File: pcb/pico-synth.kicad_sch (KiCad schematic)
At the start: 48 parts

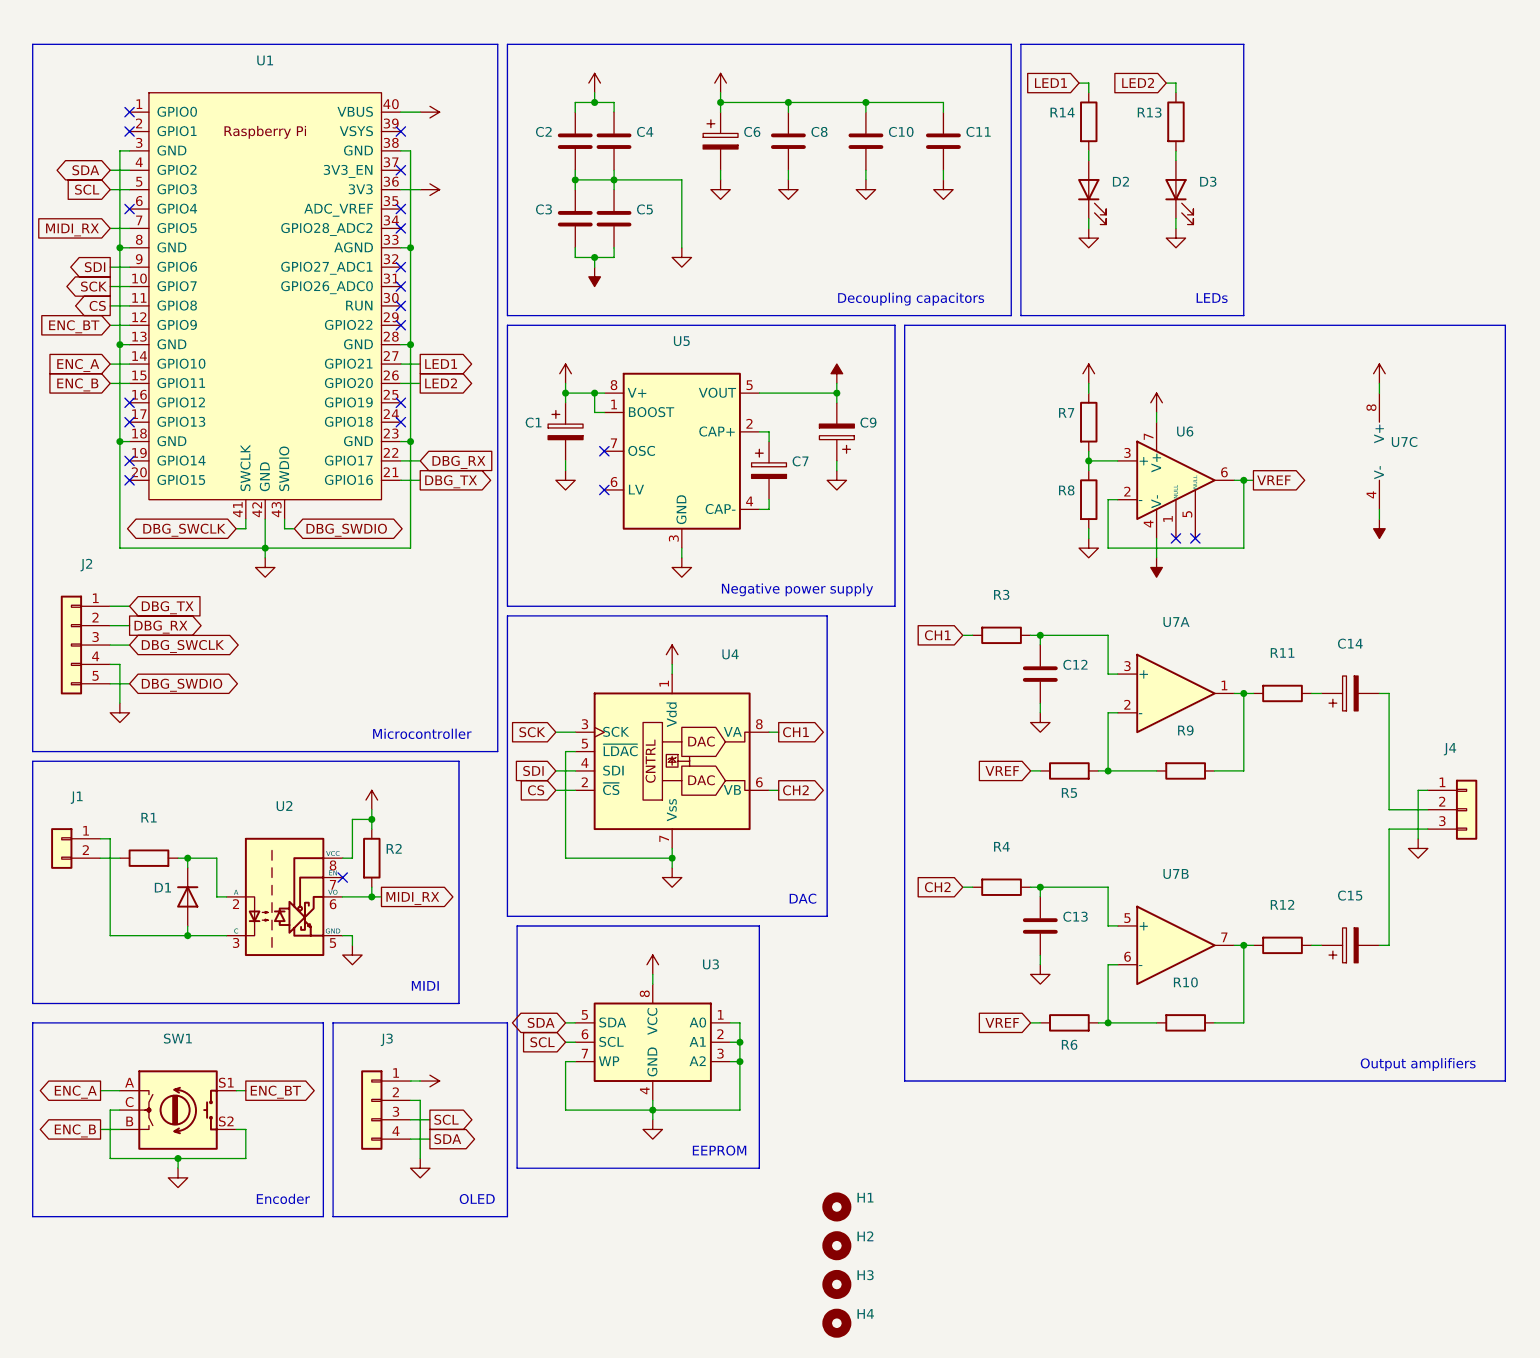
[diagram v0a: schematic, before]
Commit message: pcb: added new revision 2.2
trying to avoid using dc-dc charge pump
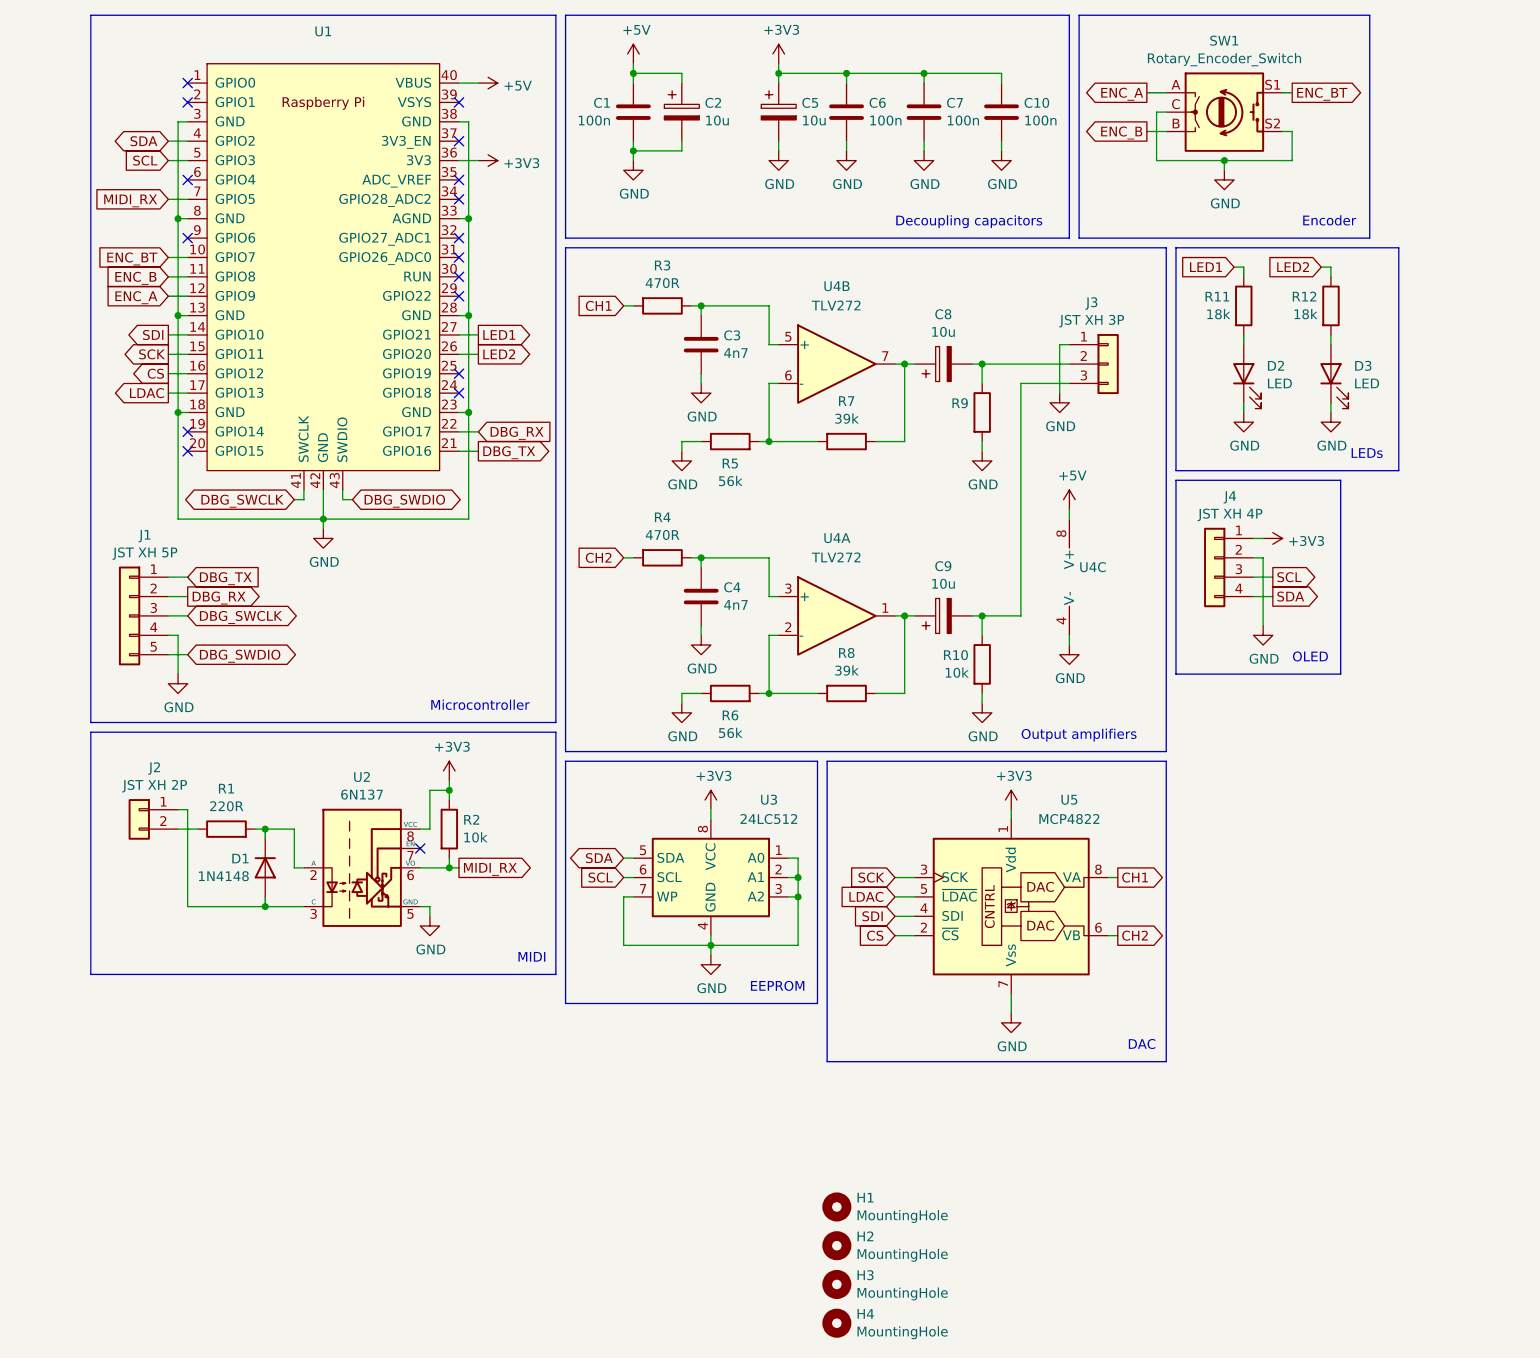
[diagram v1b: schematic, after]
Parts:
- removed C1, C14, C15, C7: (no value), symbol Device:CP
- removed C3, C4, C5: (no value), symbol Device:C
- removed R11, R12, R7, R8: (no value), symbol Device:R
- removed U5: (no value), symbol Regulator_SwitchedCapacitor:LTC1044
- removed U6: (no value), symbol Amplifier_Operational:TL071
- removed U7: (no value), symbol Amplifier_Operational:TL072
- added C2, C8: 10u, Capacitor_THT:CP_Radial_D5.0mm_P2.50mm, symbol Device:CP
- added R10: 10k, Resistor_THT:R_Axial_DIN0207_L6.3mm_D2.5mm_P10.16mm_Horizontal, symbol Device:R
- added R9: (no value), Resistor_THT:R_Axial_DIN0207_L6.3mm_D2.5mm_P10.16mm_Horizontal, symbol Device:R
- added U4: TLV272, Package_DIP:DIP-8_W7.62mm_LongPads, symbol TLV272:TLV272
- C1: renamed from C2; value (none) -> 100n; footprint (none) -> Capacitor_THT:C_Disc_D4.3mm_W1.9mm_P5.00mm
- C10: renamed from C11; value (none) -> 100n; footprint (none) -> Capacitor_THT:C_Disc_D4.3mm_W1.9mm_P5.00mm
- C3: renamed from C12; value (none) -> 4n7; footprint (none) -> Capacitor_THT:C_Disc_D3.0mm_W1.6mm_P2.50mm
- C4: renamed from C13; value (none) -> 4n7; footprint (none) -> Capacitor_THT:C_Disc_D3.0mm_W1.6mm_P2.50mm
- C5: renamed from C6; value (none) -> 10u; footprint (none) -> Capacitor_THT:CP_Radial_D5.0mm_P2.50mm
- C6: renamed from C8; value (none) -> 100n; footprint (none) -> Capacitor_THT:C_Disc_D4.3mm_W1.9mm_P5.00mm
- C7: renamed from C10; value (none) -> 100n; footprint (none) -> Capacitor_THT:C_Disc_D4.3mm_W1.9mm_P5.00mm
- C9: value (none) -> 10u; footprint (none) -> Capacitor_THT:CP_Radial_D5.0mm_P2.50mm
- D1: value (none) -> 1N4148; footprint (none) -> Diode_THT:D_DO-35_SOD27_P7.62mm_Horizontal
- D2, D3: value (none) -> LED; footprint (none) -> LED_THT:LED_D3.0mm
- H1, H2, H3, H4: value (none) -> MountingHole; footprint (none) -> MountingHole:MountingHole_2.2mm_M2_Pad_Via
- J1: renamed from J2; value (none) -> JST XH 5P; footprint (none) -> Connector_JST:JST_XH_B5B-XH-A_1x05_P2.50mm_Vertical
- J2: renamed from J1; value (none) -> JST XH 2P; footprint (none) -> Connector_JST:JST_XH_B2B-XH-A_1x02_P2.50mm_Vertical
- J3: renamed from J4; value (none) -> JST XH 3P; footprint (none) -> Connector_JST:JST_XH_B3B-XH-A_1x03_P2.50mm_Vertical
- J4: renamed from J3; value (none) -> JST XH 4P; footprint (none) -> Connector_JST:JST_XH_B4B-XH-A_1x04_P2.50mm_Vertical
- R1: value (none) -> 220R; footprint (none) -> Resistor_THT:R_Axial_DIN0207_L6.3mm_D2.5mm_P10.16mm_Horizontal
- R11: renamed from R14; value (none) -> 18k; footprint (none) -> Resistor_THT:R_Axial_DIN0207_L6.3mm_D2.5mm_P10.16mm_Horizontal
- R12: renamed from R13; value (none) -> 18k; footprint (none) -> Resistor_THT:R_Axial_DIN0207_L6.3mm_D2.5mm_P10.16mm_Horizontal
- R2: value (none) -> 10k; footprint (none) -> Resistor_THT:R_Axial_DIN0207_L6.3mm_D2.5mm_P10.16mm_Horizontal
- R3, R4: value (none) -> 470R; footprint (none) -> Resistor_THT:R_Axial_DIN0207_L6.3mm_D2.5mm_P10.16mm_Horizontal
- R5, R6: value (none) -> 56k; footprint (none) -> Resistor_THT:R_Axial_DIN0207_L6.3mm_D2.5mm_P10.16mm_Horizontal
- R7: renamed from R9; value (none) -> 39k; footprint (none) -> Resistor_THT:R_Axial_DIN0207_L6.3mm_D2.5mm_P10.16mm_Horizontal
- R8: renamed from R10; value (none) -> 39k; footprint (none) -> Resistor_THT:R_Axial_DIN0207_L6.3mm_D2.5mm_P10.16mm_Horizontal
- SW1: value (none) -> Rotary_Encoder_Switch; footprint (none) -> Rotary_Encoder:RotaryEncoder_Alps_EC11E-Switch_Vertical_H20mm_CircularMountingHoles
- U2: value (none) -> 6N137; footprint (none) -> Package_DIP:DIP-8_W7.62mm
- U3: value (none) -> 24LC512; footprint (none) -> Package_DIP:DIP-8_W7.62mm_LongPads
- U5: renamed from U4; value (none) -> MCP4822; footprint (none) -> Package_DIP:DIP-8_W7.62mm_LongPads
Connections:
- net -5V is gone; now on an unnamed net: C9.2
- net VREF is gone; now on net GND: R5.1, R6.1
- net +5V: now also C2.1, U4.8 (V+)
- net CS: now also U1.16 (GPIO12); no longer U1.11 (GPIO8)
- net ENC_A: now also U1.12 (GPIO9); no longer U1.14 (GPIO10)
- net ENC_B: now also U1.11 (GPIO8); no longer U1.15 (GPIO11)
- net ENC_BT: now also U1.10 (GPIO7); no longer U1.12 (GPIO9)
- net GND: now also C2.2, R10.2, R9.2, U4.4 (V-); no longer C9.1, U5.5 (~{LDAC})
- net SCK: now also U1.15 (GPIO11); no longer U1.10 (GPIO7)
- net SDI: now also U1.14 (GPIO10); no longer U1.9 (GPIO6)
- net at R7.1: now also C8.1, U4.7
- net at R5.2, R7.2: now also U4.6 (-)
- net at C3.1, R3.1: now also U4.5 (+)
- net at C4.1, R4.1: now also U4.3 (+)
- net at R6.2, R8.2: now also U4.2 (-)
- net at R8.1: now also C9.1, U4.1
- net at J3.2 (Pin_2): now also C8.2, R9.1
- net at J3.3 (Pin_3): now also R10.1
- net LDAC: now reaches U1.17 (GPIO13)
- net LDAC: now also U5.5 (~{LDAC})
- no-connect marks 22 -> 17
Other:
- note removed: "Negative power supply"
- moved on the sheet: C1, C10, C3, C4, C5, C6, C7, D1, D2, D3, J1, J2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

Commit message: wip
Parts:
- R9: value (none) -> 10k
- U1: value (none) -> Pico; footprint (none) -> MCU_RaspberryPi_and_Boards:RPi_Pico_SMD_TH
- U3, U4, U5: footprint Package_DIP:DIP-8_W7.62mm_LongPads -> (none)
- U4: value (none) -> TLV272
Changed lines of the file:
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@@
     (property "Reference" "U5" (id 0) (at 190.5 124.46 0))
     (property "Value" "MCP4822" (id 1) (at 190.5 127 0))
-    (property "Footprint" "Package_DIP:DIP-8_W7.62mm_LongPads" (id 2) (at 203.2 144.78 0)
+    (property "Footprint" "" (id 2) (at 203.2 144.78 0)
       (effects (font (size 1.27 1.27)) hide)
     )
@@
     (property "Reference" "U3" (id 0) (at 151.13 124.46 0))
     (property "Value" "24LC512" (id 1) (at 151.13 127 0))
-    (property "Footprint" "Package_DIP:DIP-8_W7.62mm_LongPads" (id 2) (at 143.51 134.62 0)
+    (property "Footprint" "" (id 2) (at 143.51 134.62 0)
       (effects (font (size 1.27 1.27)) hide)
     )
@@
     (in_bom yes) (on_board yes)
     (property "Reference" "U1" (id 0) (at 92.71 23.749 0))
-    (property "Value" "" (id 1) (at 92.71 26.0604 0))
-    (property "Footprint" "" (id 2) (at 92.71 54.61 90)
+    (property "Value" "Pico" (id 1) (at 92.71 26.0604 0))
+    (property "Footprint" "MCU_RaspberryPi_and_Boards:RPi_Pico_SMD_TH" (id 2) (at 92.71 54.61 90)
       (effects (font (size 1.27 1.27)) hide)
     )
@@
       (effects (font (size 1.27 1.27)) (justify right))
     )
-    (property "Value" "" (id 1) (at 177.3174 74.803 0)
+    (property "Value" "10k" (id 1) (at 177.3174 74.803 0)
       (effects (font (size 1.27 1.27)) (justify right))
     )
@@
     (property "Reference" "U4" (id 0) (at 160.02 57.15 0))
     (property "Value" "TLV272" (id 1) (at 160.02 59.69 0))
-    (property "Footprint" "Package_DIP:DIP-8_W7.62mm_LongPads" (id 2) (at 160.02 67.31 0)
+    (property "Footprint" "" (id 2) (at 160.02 67.31 0)
       (effects (font (size 1.27 1.27)) hide)
     )
@@
       (effects (font (size 1.27 1.27)) (justify left))
     )
-    (property "Value" "" (id 1) (at 191.77 96.5199 0)
+    (property "Value" "TLV272" (id 1) (at 191.77 96.5199 0)
       (effects (font (size 1.27 1.27)) (justify left))
     )
@@
     (property "Reference" "U4" (id 0) (at 160.02 90.17 0))
     (property "Value" "TLV272" (id 1) (at 160.02 92.71 0))
-    (property "Footprint" "Package_DIP:DIP-8_W7.62mm_LongPads" (id 2) (at 160.02 100.33 0)
+    (property "Footprint" "" (id 2) (at 160.02 100.33 0)
       (effects (font (size 1.27 1.27)) hide)
     )
@@
     )
     (path "/00000000-0000-0000-0000-0000610d3b82"
-      (reference "U3") (unit 1) (value "24LC512") (footprint "Package_DIP:DIP-8_W7.62mm_LongPads")
+      (reference "U3") (unit 1) (value "24LC512") (footprint "Package_DIP:DIP-8_W7.62mm")
     )
     (path "/b78ec6e1-3af4-42f0-8ebe-c8e78f2dd6c1"
-      (reference "U4") (unit 1) (value "TLV272") (footprint "Package_DIP:DIP-8_W7.62mm_LongPads")
+      (reference "U4") (unit 1) (value "TLV272") (footprint "Package_DIP:DIP-8_W7.62mm")
     )
     (path "/985f5225-3a93-44b7-b19b-c2b15ccb4687"
-      (reference "U4") (unit 2) (value "TLV272") (footprint "Package_DIP:DIP-8_W7.62mm_LongPads")
+      (reference "U4") (unit 2) (value "TLV272") (footprint "Package_DIP:DIP-8_W7.62mm")
     )
     (path "/a474d9a7-6ee3-418d-817c-a749fb38714c"
-      (reference "U4") (unit 3) (value "TLV272") (footprint "Package_DIP:DIP-8_W7.62mm_LongPads")
+      (reference "U4") (unit 3) (value "TLV272") (footprint "Package_DIP:DIP-8_W7.62mm")
     )
     (path "/00000000-0000-0000-0000-000060d64751"
-      (reference "U5") (unit 1) (value "MCP4822") (footprint "Package_DIP:DIP-8_W7.62mm_LongPads")
-    )
-  )
+      (reference "U5") (unit 1) (value "MCP4822") (footprint "Package_DIP:DIP-8_W7.62mm")
+    )
+  )
